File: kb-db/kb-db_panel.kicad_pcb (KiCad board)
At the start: 2 copper layers, 42 x 23 mm, 28 parts, among them J1 Conn_01x04

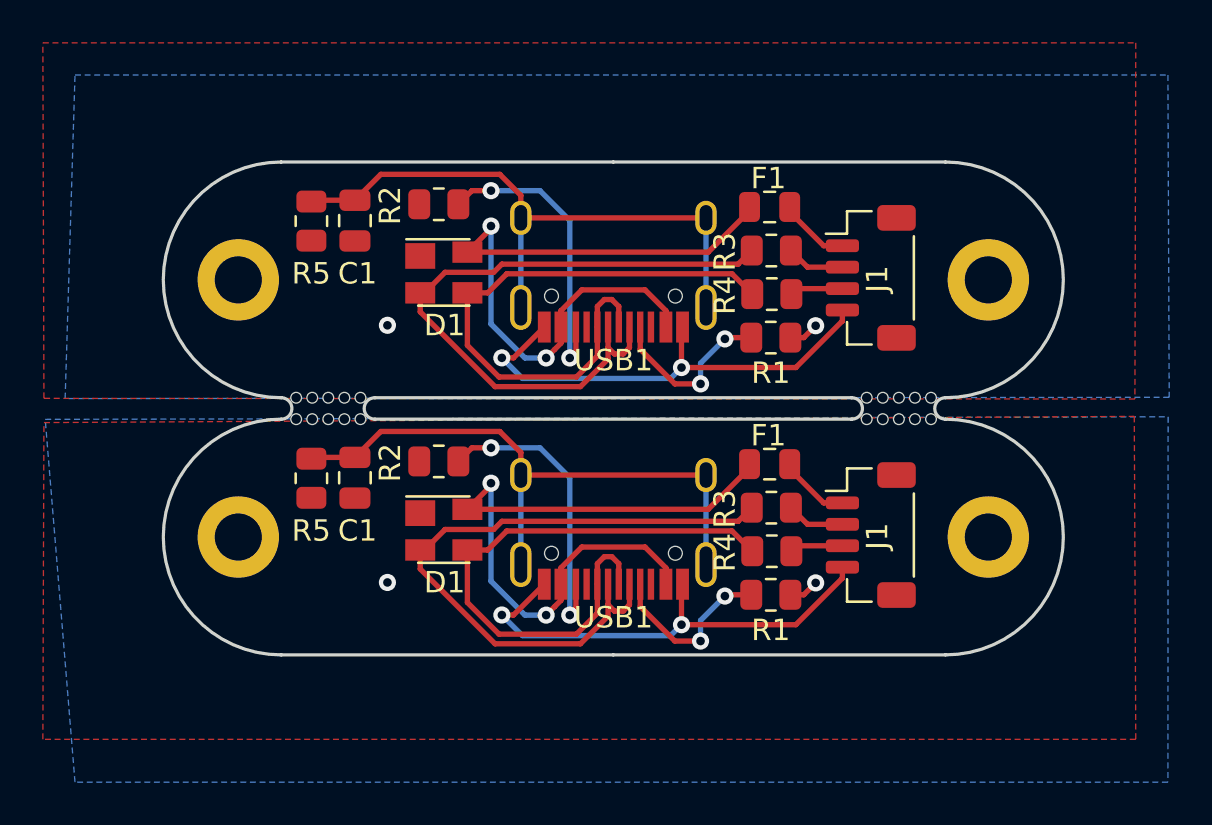
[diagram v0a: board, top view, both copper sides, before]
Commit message: Ground components to USB ground
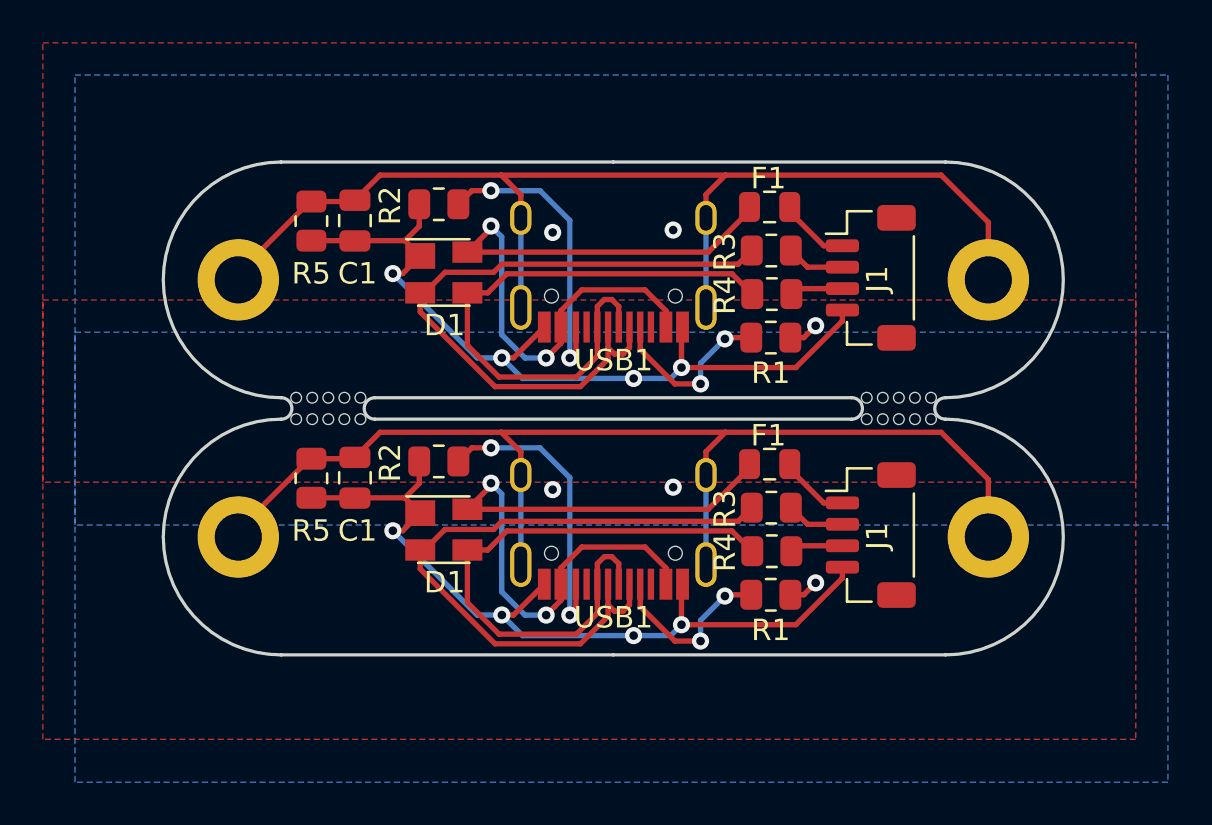
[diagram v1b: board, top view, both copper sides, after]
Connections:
- C1 pad 1: Net-(C1-Pad1) -> (no net)
- C1 pad 2: Earth -> (no net)
- C1 pad 1: Net-(C1-Pad1) -> Earth
- C1 pad 2: Earth -> GND
- D1 pad 1: Earth -> (no net)
- D1 pad 2: DBUS- -> (no net)
- D1 pad 3: DBUS+ -> (no net)
- D1 pad 4: VCC -> (no net)
- D1 pad 1: Earth -> GND
- F1 pad 1: +5V -> (no net)
- F1 pad 2: VCC -> (no net)
- H1 pad 1: Earth -> (no net)
- H2 pad 1: Earth -> (no net)
- J1 pad 1: +5V -> (no net)
- J1 pad 2: D- -> (no net)
- J1 pad 3: D+ -> (no net)
- J1 pad 4: GND -> (no net)
- R1 pad 1: Earth -> (no net)
- R1 pad 2: Net-(R1-Pad2) -> (no net)
- R1 pad 1: Earth -> GND
- R2 pad 1: Earth -> (no net)
- R2 pad 2: Net-(R2-Pad2) -> (no net)
- R2 pad 1: Earth -> GND
- R3 pad 1: D- -> (no net)
- R3 pad 2: DBUS- -> (no net)
- R4 pad 1: D+ -> (no net)
- R4 pad 2: DBUS+ -> (no net)
- R5 pad 1: Net-(C1-Pad1) -> (no net)
- R5 pad 2: Earth -> (no net)
- R5 pad 1: Net-(C1-Pad1) -> Earth
- R5 pad 2: Earth -> GND
- USB1 pad 1: GND -> (no net)
- USB1 pad 10: Net-(R2-Pad2) -> (no net)
- USB1 pad 11: VCC -> (no net)
- USB1 pad 12: GND -> (no net)
- USB1 pad 13: Net-(C1-Pad1) -> (no net)
- USB1 pad 2: VCC -> (no net)
- USB1 pad 3: Net-(USB1-Pad3) -> (no net)
- USB1 pad 4: Net-(R1-Pad2) -> (no net)
- USB1 pad 5: DBUS- -> (no net)
- USB1 pad 6: DBUS+ -> (no net)
- USB1 pad 7: DBUS- -> (no net)
- USB1 pad 8: DBUS+ -> (no net)
- USB1 pad 9: Net-(USB1-Pad9) -> (no net)
- USB1 pad 13: Net-(C1-Pad1) -> Earth
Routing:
- net (no net): track 0.00 -> 216.6 mm, vias 0 -> 13
- net Net-(C1-Pad1): track 57.5 -> 0.00 mm
- net Earth: track 2.82 -> 53.9 mm, vias 4 -> 0
- net VCC: track 65.1 -> 32.6 mm, vias 4 -> 2
- net DBUS-: track 63.2 -> 31.6 mm
- net DBUS+: track 56.3 -> 28.1 mm
- net Net-(R2-Pad2): track 28.0 -> 14.0 mm, vias 4 -> 2
- net Net-(R1-Pad2): track 16.7 -> 8.35 mm, vias 4 -> 2
- net GND: track 44.8 -> 39.5 mm, vias 4 -> 7
- net +5V: track 6.68 -> 3.34 mm
- net D-: track 5.45 -> 2.73 mm
- net D+: track 4.97 -> 2.49 mm
- added copper zone on B.Cu, net (none)
- added copper zone on F.Cu, net (none)
- added copper zone on B.Cu, net GND
- added copper zone on F.Cu, net GND
- removed copper zone on B.Cu, net Earth
- removed copper zone on F.Cu, net Earth
